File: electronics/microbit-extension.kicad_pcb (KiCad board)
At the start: 2 copper layers, 43.2 x 59.7 mm, 31 parts, among them J1 microbit_edge_connector, J2 9V conn, SW1 SW_DIP_x01, SW2 SW_DIP_x01, SW3 SW_DIP_x01, SW4 SW_DIP_x01, T1 2N4401, U1 LD1117S33CTR

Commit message: finished up routing
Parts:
- moved T1 6.61 mm to (70.9, 113.0)
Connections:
- T1 pad 1: (no net) -> Net-(R9-Pad1)
- T1 pad 2: (no net) -> Net-(BZ1-Pad2)
- T1 pad 3: (no net) -> GND
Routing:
- net Net-(R9-Pad1): track 0.00 -> 48.6 mm, vias 0 -> 2
- net /BUZZER_PIN: track 0.00 -> 16.8 mm, vias 0 -> 2
- net Net-(BZ1-Pad2): track 0.00 -> 9.27 mm
- net GND: track 183.3 -> 188.4 mm, vias 7 -> 8
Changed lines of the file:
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@@
 (kicad_pcb (version 4) (host pcbnew 4.0.6)
   (general
-    (links 80)
-    (no_connects 3)
+    (links 83)
+    (no_connects 2)
     (area 43.739999 68.504999 87.070001 128.345001)
     (thickness 1.6)
     (drawings 5)
-    (tracks 370)
+    (tracks 403)
     (zones 0)
     (modules 31)
@@
   )
   (module TO_SOT_Packages_SMD:SOT-23 (layer F.Cu)
-    (at 71.12 119.634)
+    (at 70.866 113.03)
     (descr "SOT-23, Standard")
     (tags SOT-23)
@@
     (fp_line (start 0.76 -1.58) (end -1.4 -1.58) (layer F.SilkS) (width 0.12))
     (fp_line (start 0.76 1.58) (end -0.7 1.58) (layer F.SilkS) (width 0.12))
-    (pad 1 smd rect (at -1 -0.95) (size 0.9 0.8) (layers F.Cu F.Paste F.Mask))
-    (pad 2 smd rect (at -1 0.95) (size 0.9 0.8) (layers F.Cu F.Paste F.Mask))
-    (pad 3 smd rect (at 1 0) (size 0.9 0.8) (layers F.Cu F.Paste F.Mask))
+    (pad 1 smd rect (at -1 -0.95) (size 0.9 0.8) (layers F.Cu F.Paste F.Mask)
+      (net 72 "Net-(R9-Pad1)"))
+    (pad 2 smd rect (at -1 0.95) (size 0.9 0.8) (layers F.Cu F.Paste F.Mask)
+      (net 1 "Net-(BZ1-Pad2)"))
+    (pad 3 smd rect (at 1 0) (size 0.9 0.8) (layers F.Cu F.Paste F.Mask)
+      (net 4 GND))
     (model ${KISYS3DMOD}/TO_SOT_Packages_SMD.3dshapes/SOT-23.wrl
       (at (xyz 0 0 0))
@@
   (gr_line (start 86.995 68.58) (end 86.995 128.27) (angle 90) (layer Edge.Cuts) (width 0.15))
   (gr_line (start 44.45 68.58) (end 86.995 68.58) (angle 90) (layer Edge.Cuts) (width 0.15))
+  (segment (start 69.866 113.98) (end 71.562 113.98) (width 0.25) (layer F.Cu) (net 1) (status 400000))
+  (segment (start 72.517 114.935) (end 78.74 114.935) (width 0.25) (layer F.Cu) (net 1) (status 800000))
+  (segment (start 71.562 113.98) (end 72.517 114.935) (width 0.25) (layer F.Cu) (net 1))
   (segment (start 82.296 75.946) (end 83.82 75.946) (width 0.25) (layer F.Cu) (net 2))
-  (segment (start 84.328 76.454) (end 84.328 77.486) (width 0.25) (layer F.Cu) (net 2) (status 800000))
+  (segment (start 84.328 76.454) (end 84.328 77.486) (width 0.25) (layer F.Cu) (net 2))
   (segment (start 83.82 75.946) (end 84.328 76.454) (width 0.25) (layer F.Cu) (net 2))
   (segment (start 82.55 94.234) (end 82.55 90.678) (width 0.25) (layer F.Cu) (net 2))
@@
   (segment (start 83.058 78.74) (end 83.312 78.486) (width 0.25) (layer F.Cu) (net 2))
   (segment (start 83.312 78.486) (end 83.328 78.486) (width 0.25) (layer F.Cu) (net 2))
-  (segment (start 83.328 78.486) (end 84.328 77.486) (width 0.25) (layer F.Cu) (net 2) (status 800000))
+  (segment (start 83.328 78.486) (end 84.328 77.486) (width 0.25) (layer F.Cu) (net 2))
   (segment (start 84.328 77.486) (end 84.09 77.486) (width 0.25) (layer F.Cu) (net 2))
   (segment (start 82.55 75.946) (end 82.296 75.946) (width 0.25) (layer F.Cu) (net 2))
@@
   (segment (start 85.598 75.946) (end 85.598 89.75) (width 0.25) (layer F.Cu) (net 3))
   (segment (start 84.836 75.184) (end 85.598 75.946) (width 0.25) (layer F.Cu) (net 3))
+  (segment (start 66.802 113.157) (end 70.739 113.157) (width 0.25) (layer B.Cu) (net 4) (status 400000))
+  (segment (start 70.866 113.03) (end 71.866 113.03) (width 0.25) (layer F.Cu) (net 4) (status 800000))
+  (via (at 70.866 113.03) (size 0.6) (drill 0.4) (layers F.Cu B.Cu) (net 4))
+  (segment (start 70.739 113.157) (end 70.866 113.03) (width 0.25) (layer B.Cu) (net 4))
   (segment (start 84.836 70.612) (end 83.82 70.612) (width 0.25) (layer B.Cu) (net 4))
   (segment (start 82.804 71.628) (end 82.804 72.644) (width 0.25) (layer B.Cu) (net 4))
@@
   (segment (start 48.26 78.74) (end 49.53 78.74) (width 0.25) (layer F.Cu) (net 37))
   (segment (start 49.53 78.74) (end 49.53 76.2) (width 0.25) (layer F.Cu) (net 37))
+  (segment (start 62.926 75.946) (end 62.926 76.52) (width 0.25) (layer F.Cu) (net 38) (status C00000))
+  (segment (start 62.926 76.52) (end 62.484 76.962) (width 0.25) (layer F.Cu) (net 38) (status 400000))
+  (segment (start 62.484 76.962) (end 60.198 76.962) (width 0.25) (layer F.Cu) (net 38))
+  (via (at 60.198 76.962) (size 0.6) (drill 0.4) (layers F.Cu B.Cu) (net 38))
+  (segment (start 60.198 76.962) (end 59.944 76.708) (width 0.25) (layer B.Cu) (net 38))
+  (segment (start 59.944 76.708) (end 59.944 74.93) (width 0.25) (layer B.Cu) (net 38))
+  (via (at 59.944 74.93) (size 0.6) (drill 0.4) (layers F.Cu B.Cu) (net 38))
+  (segment (start 59.944 74.93) (end 59.69 74.676) (width 0.25) (layer F.Cu) (net 38))
+  (segment (start 59.69 74.676) (end 55.88 74.676) (width 0.25) (layer F.Cu) (net 38))
+  (segment (start 55.88 74.676) (end 55.626 74.93) (width 0.25) (layer F.Cu) (net 38))
+  (segment (start 55.626 74.93) (end 54.102 74.93) (width 0.25) (layer F.Cu) (net 38))
+  (segment (start 54.102 74.93) (end 52.832 73.66) (width 0.25) (layer F.Cu) (net 38))
+  (segment (start 52.832 73.66) (end 49.53 73.66) (width 0.25) (layer F.Cu) (net 38) (status 800000))
   (segment (start 46.99 95.25) (end 46.736 95.25) (width 0.25) (layer B.Cu) (net 39))
   (segment (start 46.736 95.25) (end 44.958 97.028) (width 0.25) (layer B.Cu) (net 39))
@@
   (segment (start 78.552 70.866) (end 78.806 70.612) (width 0.25) (layer F.Cu) (net 52))
   (segment (start 63.976 79.67) (end 63.976 85.43) (width 0.25) (layer F.Cu) (net 52))
+  (segment (start 69.866 112.08) (end 69.866 111.776) (width 0.25) (layer F.Cu) (net 72) (status C00000))
+  (segment (start 69.866 111.776) (end 68.326 110.236) (width 0.25) (layer F.Cu) (net 72) (status 400000))
+  (via (at 68.326 110.236) (size 0.6) (drill 0.4) (layers F.Cu B.Cu) (net 72))
+  (segment (start 68.326 110.236) (end 67.818 109.728) (width 0.25) (layer B.Cu) (net 72))
+  (segment (start 67.818 109.728) (end 58.674 109.728) (width 0.25) (layer B.Cu) (net 72))
+  (segment (start 58.674 109.728) (end 57.658 108.712) (width 0.25) (layer B.Cu) (net 72))
+  (segment (start 57.658 108.712) (end 57.658 101.6) (width 0.25) (layer B.Cu) (net 72))
+  (segment (start 57.658 101.6) (end 58.674 100.584) (width 0.25) (layer B.Cu) (net 72))
+  (segment (start 58.674 100.584) (end 58.674 89.408) (width 0.25) (layer B.Cu) (net 72))
+  (via (at 58.674 89.408) (size 0.6) (drill 0.4) (layers F.Cu B.Cu) (net 72))
+  (segment (start 58.674 89.408) (end 58.674 77.216) (width 0.25) (layer F.Cu) (net 72))
+  (segment (start 58.674 77.216) (end 59.944 75.946) (width 0.25) (layer F.Cu) (net 72))
+  (segment (start 59.944 75.946) (end 61.026 75.946) (width 0.25) (layer F.Cu) (net 72) (status 800000))
 )

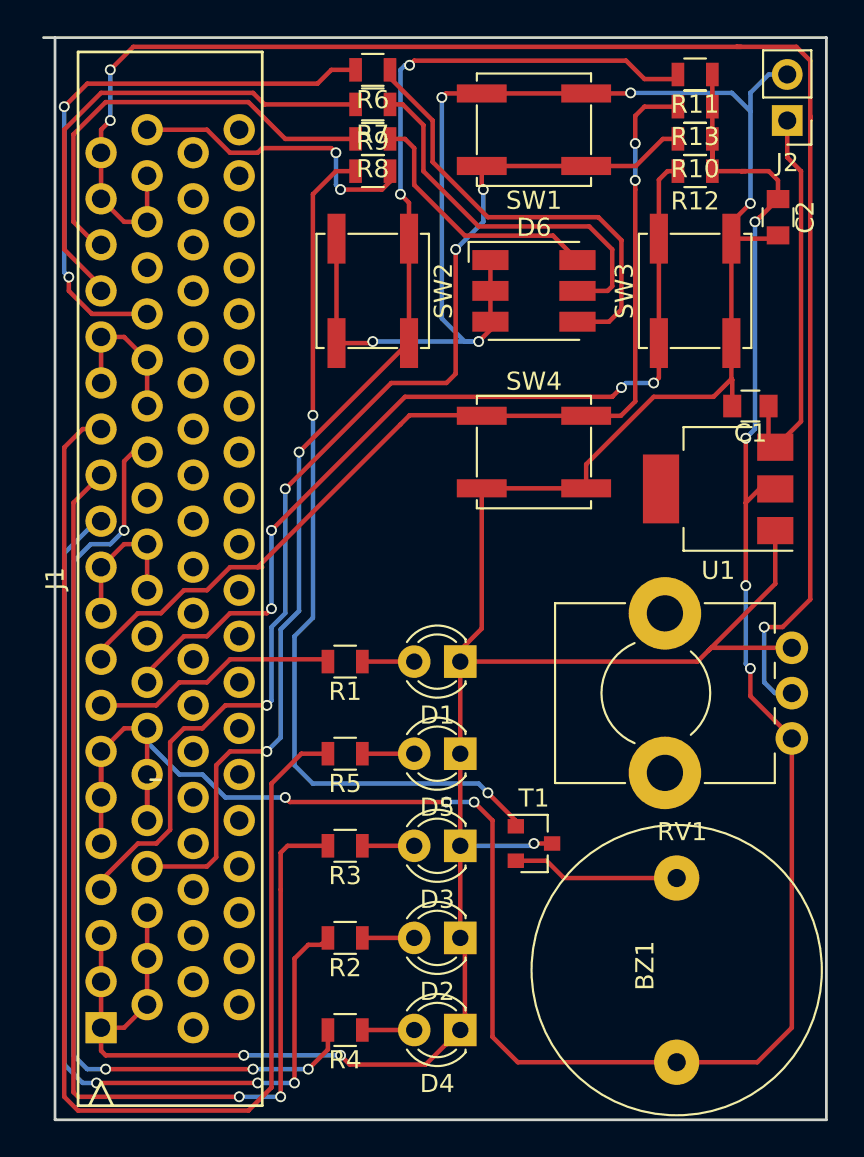
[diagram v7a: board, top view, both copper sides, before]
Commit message: added copperpours
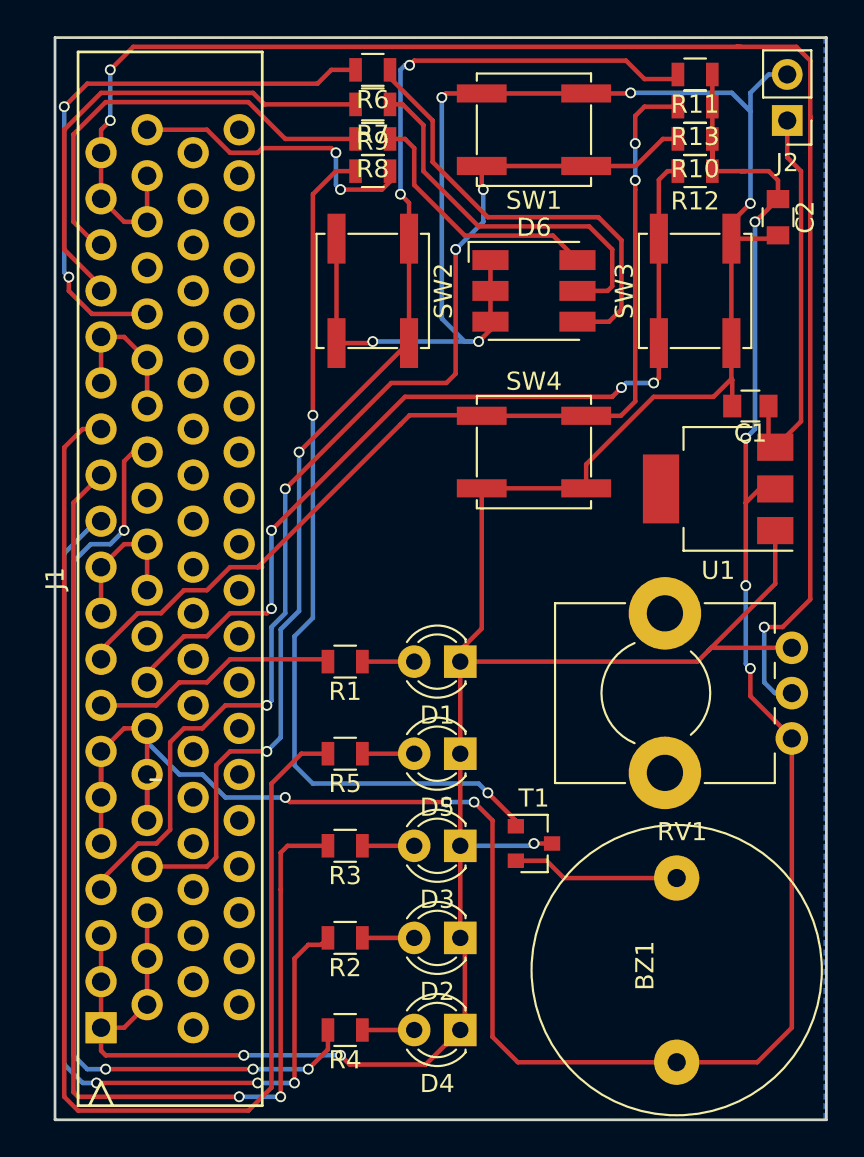
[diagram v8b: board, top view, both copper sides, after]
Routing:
- added copper zone on B.Cu, net GND
- added copper zone on F.Cu, net GND
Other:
- board size 43.2 x 59.7 mm -> 42.5 x 59.7 mm
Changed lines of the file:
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@@
   (general
     (links 83)
-    (no_connects 2)
-    (area 43.739999 68.504999 87.070001 128.345001)
+    (no_connects 1)
+    (area 44.374999 68.504999 87.070001 128.345001)
     (thickness 1.6)
-    (drawings 5)
+    (drawings 4)
     (tracks 403)
     (zones 0)
@@
     )
   )
-  (gr_line (start 44.45 68.58) (end 43.815 68.58) (angle 90) (layer Edge.Cuts) (width 0.15))
   (gr_line (start 44.45 128.27) (end 44.45 68.58) (angle 90) (layer Edge.Cuts) (width 0.15))
   (gr_line (start 86.995 128.27) (end 44.45 128.27) (angle 90) (layer Edge.Cuts) (width 0.15))
   (gr_line (start 86.995 68.58) (end 86.995 128.27) (angle 90) (layer Edge.Cuts) (width 0.15))
   (gr_line (start 44.45 68.58) (end 86.995 68.58) (angle 90) (layer Edge.Cuts) (width 0.15))
-  (segment (start 69.866 113.98) (end 71.562 113.98) (width 0.25) (layer F.Cu) (net 1) (status 400000))
-  (segment (start 72.517 114.935) (end 78.74 114.935) (width 0.25) (layer F.Cu) (net 1) (status 800000))
+  (segment (start 69.866 113.98) (end 71.562 113.98) (width 0.25) (layer F.Cu) (net 1))
+  (segment (start 72.517 114.935) (end 78.74 114.935) (width 0.25) (layer F.Cu) (net 1))
   (segment (start 71.562 113.98) (end 72.517 114.935) (width 0.25) (layer F.Cu) (net 1))
   (segment (start 82.296 75.946) (end 83.82 75.946) (width 0.25) (layer F.Cu) (net 2))
@@
   (segment (start 85.598 75.946) (end 85.598 89.75) (width 0.25) (layer F.Cu) (net 3))
   (segment (start 84.836 75.184) (end 85.598 75.946) (width 0.25) (layer F.Cu) (net 3))
-  (segment (start 66.802 113.157) (end 70.739 113.157) (width 0.25) (layer B.Cu) (net 4) (status 400000))
-  (segment (start 70.866 113.03) (end 71.866 113.03) (width 0.25) (layer F.Cu) (net 4) (status 800000))
+  (segment (start 66.802 113.157) (end 70.739 113.157) (width 0.25) (layer B.Cu) (net 4))
+  (segment (start 70.866 113.03) (end 71.866 113.03) (width 0.25) (layer F.Cu) (net 4))
   (via (at 70.866 113.03) (size 0.6) (drill 0.4) (layers F.Cu B.Cu) (net 4))
   (segment (start 70.739 113.157) (end 70.866 113.03) (width 0.25) (layer B.Cu) (net 4))
@@
   (segment (start 48.26 78.74) (end 49.53 78.74) (width 0.25) (layer F.Cu) (net 37))
   (segment (start 49.53 78.74) (end 49.53 76.2) (width 0.25) (layer F.Cu) (net 37))
-  (segment (start 62.926 75.946) (end 62.926 76.52) (width 0.25) (layer F.Cu) (net 38) (status C00000))
-  (segment (start 62.926 76.52) (end 62.484 76.962) (width 0.25) (layer F.Cu) (net 38) (status 400000))
+  (segment (start 62.926 75.946) (end 62.926 76.52) (width 0.25) (layer F.Cu) (net 38))
+  (segment (start 62.926 76.52) (end 62.484 76.962) (width 0.25) (layer F.Cu) (net 38))
   (segment (start 62.484 76.962) (end 60.198 76.962) (width 0.25) (layer F.Cu) (net 38))
   (via (at 60.198 76.962) (size 0.6) (drill 0.4) (layers F.Cu B.Cu) (net 38))
@@
   (segment (start 55.626 74.93) (end 54.102 74.93) (width 0.25) (layer F.Cu) (net 38))
   (segment (start 54.102 74.93) (end 52.832 73.66) (width 0.25) (layer F.Cu) (net 38))
-  (segment (start 52.832 73.66) (end 49.53 73.66) (width 0.25) (layer F.Cu) (net 38) (status 800000))
+  (segment (start 52.832 73.66) (end 49.53 73.66) (width 0.25) (layer F.Cu) (net 38))
   (segment (start 46.99 95.25) (end 46.736 95.25) (width 0.25) (layer B.Cu) (net 39))
   (segment (start 46.736 95.25) (end 44.958 97.028) (width 0.25) (layer B.Cu) (net 39))
@@
   (segment (start 78.552 70.866) (end 78.806 70.612) (width 0.25) (layer F.Cu) (net 52))
   (segment (start 63.976 79.67) (end 63.976 85.43) (width 0.25) (layer F.Cu) (net 52))
-  (segment (start 69.866 112.08) (end 69.866 111.776) (width 0.25) (layer F.Cu) (net 72) (status C00000))
-  (segment (start 69.866 111.776) (end 68.326 110.236) (width 0.25) (layer F.Cu) (net 72) (status 400000))
+  (segment (start 69.866 112.08) (end 69.866 111.776) (width 0.25) (layer F.Cu) (net 72))
+  (segment (start 69.866 111.776) (end 68.326 110.236) (width 0.25) (layer F.Cu) (net 72))
   (via (at 68.326 110.236) (size 0.6) (drill 0.4) (layers F.Cu B.Cu) (net 72))
   (segment (start 68.326 110.236) (end 67.818 109.728) (width 0.25) (layer B.Cu) (net 72))
@@
   (segment (start 58.674 89.408) (end 58.674 77.216) (width 0.25) (layer F.Cu) (net 72))
   (segment (start 58.674 77.216) (end 59.944 75.946) (width 0.25) (layer F.Cu) (net 72))
-  (segment (start 59.944 75.946) (end 61.026 75.946) (width 0.25) (layer F.Cu) (net 72) (status 800000))
+  (segment (start 59.944 75.946) (end 61.026 75.946) (width 0.25) (layer F.Cu) (net 72))
+  (zone (net 4) (net_name GND) (layer B.Cu) (hatch edge 0.508)
+    (connect_pads (clearance 0.508))
+    (min_thickness 0.254)
+    (fill yes (arc_segments 16) (thermal_gap 0.508) (thermal_bridge_width 0.508))
+    (polygon
+      (pts
+        (xy 86.868 128.27) (xy 44.45 128.27) (xy 44.45 68.58) (xy 86.868 68.58)
+      )
+    )
+  )
+  (zone (net 4) (net_name GND) (layer F.Cu) (hatch edge 0.508)
+    (connect_pads (clearance 0.508))
+    (min_thickness 0.254)
+    (fill yes (arc_segments 16) (thermal_gap 0.508) (thermal_bridge_width 0.508))
+    (polygon
+      (pts
+        (xy 86.995 128.2954) (xy 44.45 128.27) (xy 44.45 68.58) (xy 86.9696 68.58)
+      )
+    )
+  )
 )
